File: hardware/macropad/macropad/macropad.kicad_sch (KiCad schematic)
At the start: 2 parts

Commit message: added some things like power
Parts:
- removed SW1: ~, keyboard_footprint:SW_UNIVERSAL_1.00u, symbol Keyboard Library:Keyboard_Push
- removed SW2: ~, keyboard_footprint:SW_UNIVERSAL_2.25u, symbol Keyboard Library:Keyboard_Push
- added C1, C2: C, symbol Device:C
- added D1: D_Schottky, symbol Device:D_Schottky
- added Q1: PMOS, symbol Simulation_SPICE:PMOS
- added U1: NRF24L01_Breakout, RF_Module:nRF24L01_Breakout, symbol RF:NRF24L01_Breakout
- added U2: AP2112K-3.3, Package_TO_SOT_SMD:SOT-23-5, symbol Regulator_Linear:AP2112K-3.3
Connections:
- new net +3.3V: C1.1, U2.5 (VOUT)
- new net BAT_OUT: Q1.1 (D)
- new net GND: C1.2, C2.2, U2.2 (GND)
- new net VBUS: D1.2 (A), Q1.2 (G)
- new net VDD: C2.1, D1.1 (K), Q1.3 (S), U2.1 (VIN)

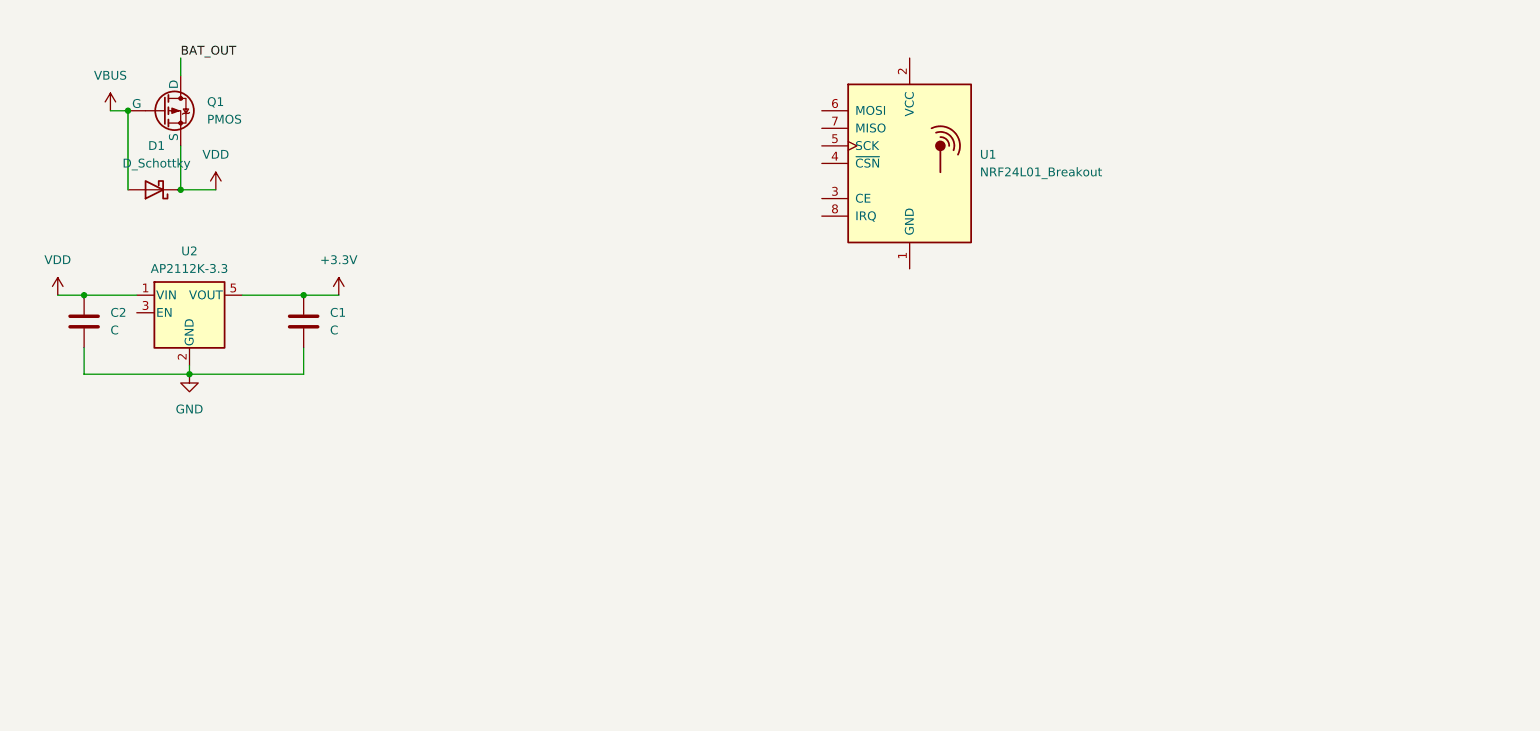
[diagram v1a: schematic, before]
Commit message: peripherals connected passive,keys still to be done
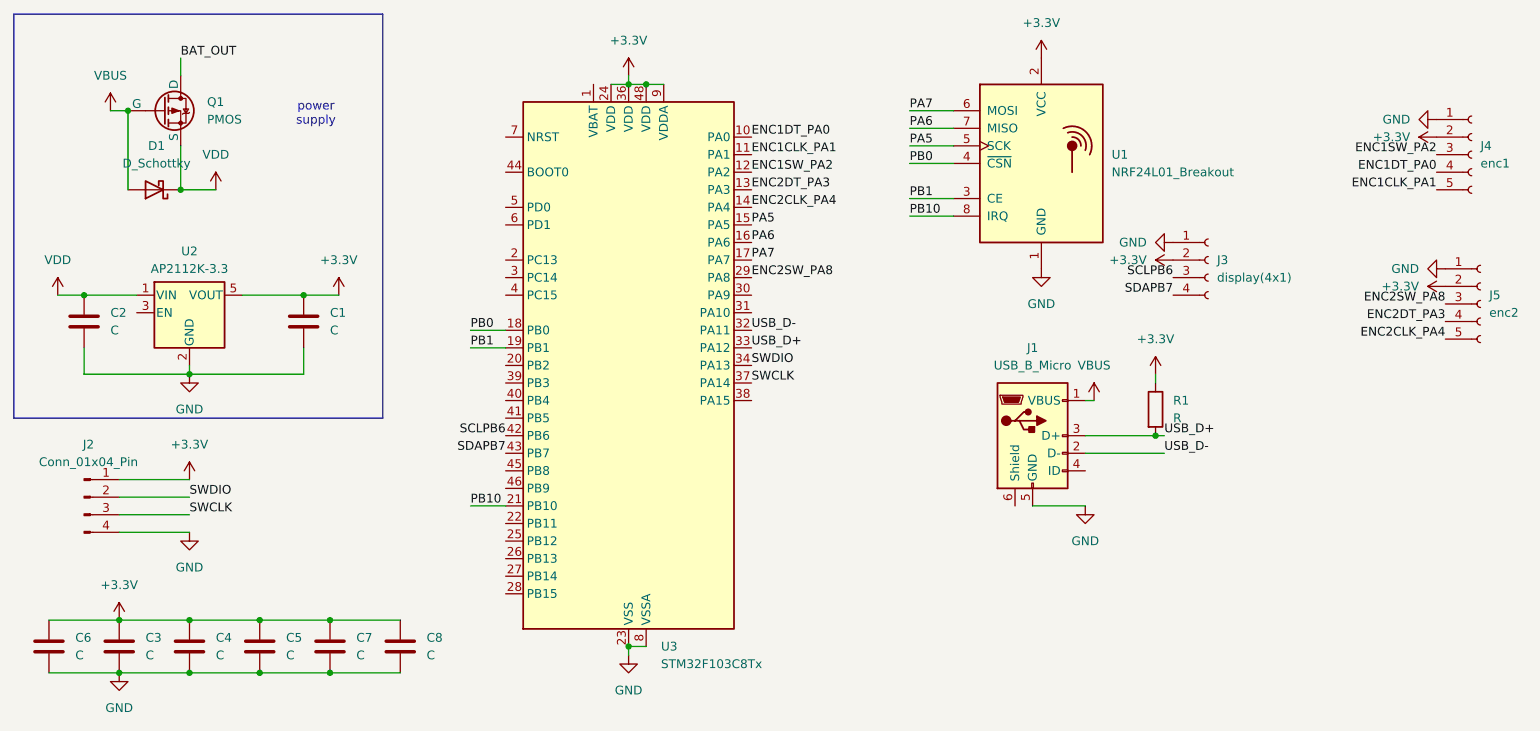
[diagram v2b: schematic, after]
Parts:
- added C3, C4, C5, C6, C7, C8: C, symbol Device:C
- added J1: USB_B_Micro, symbol Connector:USB_B_Micro
- added J2: Conn_01x04_Pin, Connector:Tag-Connect_TC2030-IDC-NL_2x03_P1.27mm_Vertical, symbol Connector:Conn_01x04_Pin
- added J3: display(4x1), symbol Connector:Conn_01x04_Socket
- added J4: enc1, symbol Connector:Conn_01x05_Socket
- added J5: enc2, symbol Connector:Conn_01x05_Socket
- added R1: R, symbol Device:R
- added U3: STM32F103C8Tx, Package_QFP:LQFP-48_7x7mm_P0.5mm, symbol MCU_ST_STM32F1:STM32F103C8Tx
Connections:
- net +3.3V: now also U1.2 (VCC), C3.1, C4.1, C5.1, C6.1, C7.1, C8.1, J2.1 (Pin_1), J3.2 (Pin_2), J4.2 (Pin_2), J5.2 (Pin_2), R1.1, U3.24 (VDD), U3.36 (VDD), U3.48 (VDD), U3.9 (VDDA)
- net GND: now also U1.1 (GND), C3.2, C4.2, C5.2, C6.2, C7.2, C8.2, J1.5 (GND), J2.4 (Pin_4), J3.1 (Pin_1), J4.1 (Pin_1), J5.1 (Pin_1), U3.23 (VSS), U3.35 (VSS), U3.47 (VSS), U3.8 (VSSA)
- net VBUS: now also J1.1 (VBUS)
- net PB1: now reaches U1.3 (CE)
- net PB1: now also U3.19 (PB1)
- net PB0: now reaches U1.4 (~{CSN})
- net PB0: now also U3.18 (PB0)
- net PA5: now reaches U1.5 (SCK)
- net PA5: now also U3.15 (PA5)
- net PA7: now reaches U1.6 (MOSI)
- net PA7: now also U3.17 (PA7)
- net PA6: now reaches U1.7 (MISO)
- net PA6: now also U3.16 (PA6)
- net PB10: now reaches U1.8 (IRQ)
- net PB10: now also U3.21 (PB10)
- new net ENC1CLK_PA1: J4.5 (Pin_5), U3.11 (PA1)
- new net ENC1DT_PA0: J4.4 (Pin_4), U3.10 (PA0)
- new net ENC1SW_PA2: J4.3 (Pin_3), U3.12 (PA2)
- new net ENC2CLK_PA4: J5.5 (Pin_5), U3.14 (PA4)
- new net ENC2DT_PA3: J5.4 (Pin_4), U3.13 (PA3)
- new net ENC2SW_PA8: J5.3 (Pin_3), U3.29 (PA8)
- new net SCLPB6: J3.3 (Pin_3), U3.42 (PB6)
- new net SDAPB7: J3.4 (Pin_4), U3.43 (PB7)
- new net SWCLK: J2.3 (Pin_3), U3.37 (PA14)
- new net SWDIO: J2.2 (Pin_2), U3.34 (PA13)
- new net USB_D+: J1.3 (D+), R1.2, U3.33 (PA12)
- new net USB_D-: J1.2 (D-), U3.32 (PA11)
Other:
- note added: "power supply"
- moved on the sheet: U1
